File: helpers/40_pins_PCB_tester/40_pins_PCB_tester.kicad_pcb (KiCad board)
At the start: 2 copper layers, 74 x 43 mm, 55 parts, among them J1 XKTF-005, J2 Conn_01x08_Socket, U1 ED078KH6

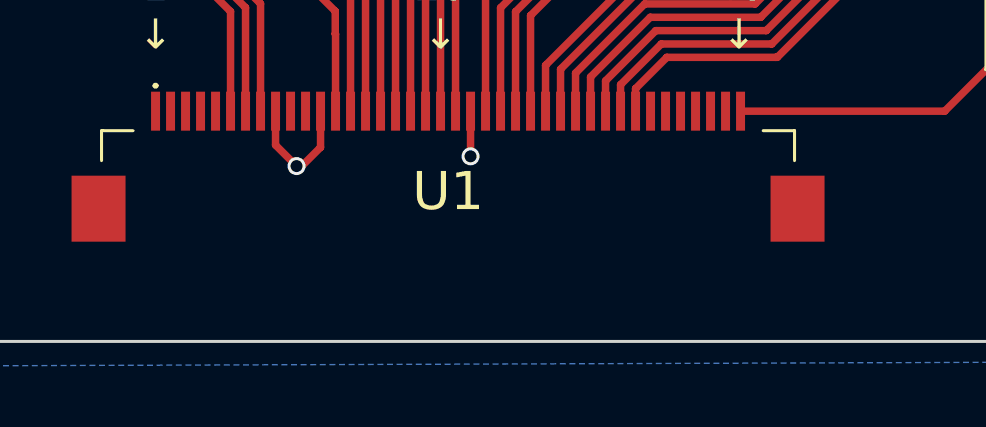
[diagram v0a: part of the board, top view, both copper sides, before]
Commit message: Add silk mentioning that needs a 40 pin Reverse FPC
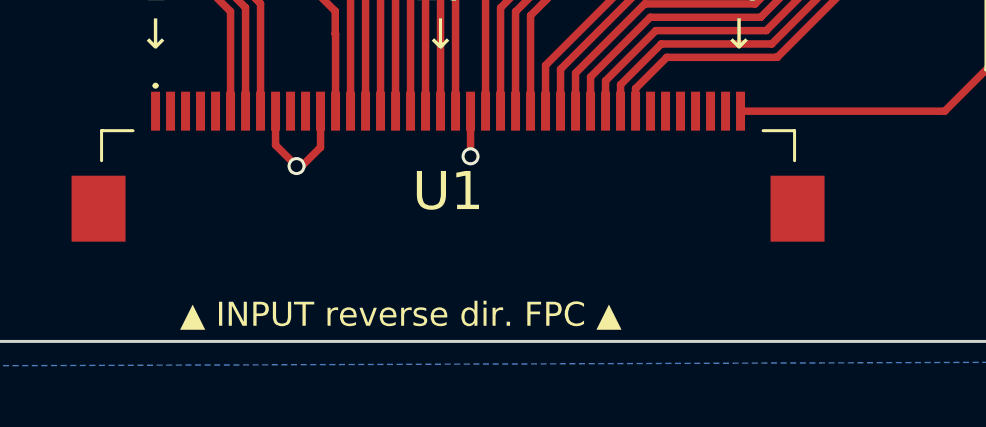
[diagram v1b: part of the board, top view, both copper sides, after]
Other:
- board text added: "▲ INPUT reverse dir. FPC ▲"
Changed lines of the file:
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@@
     (effects (font (size 1 1) (thickness 0.15)) (justify bottom))
+  )
+  (gr_text "▲ INPUT reverse dir. FPC ▲" (at 84.725 100.575) (layer "F.SilkS")
+    (effects (font (size 0.8 0.8) (thickness 0.15)) (justify left bottom))
   )
   (gr_text "MicroSD module test" (at 124.05 75.875) (layer "F.SilkS")
